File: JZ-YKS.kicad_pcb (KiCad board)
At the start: 2 copper layers, 50 x 50 mm, 50 parts, among them IC1 JZ4725, J1 USB_MINIB, U1 PINHEAD30, U2 PINHEAD30, U4 HY27UG088G5M, U5 P3V56S40ETP-G6, X1 CRYSTAL, X2 CRYSTAL

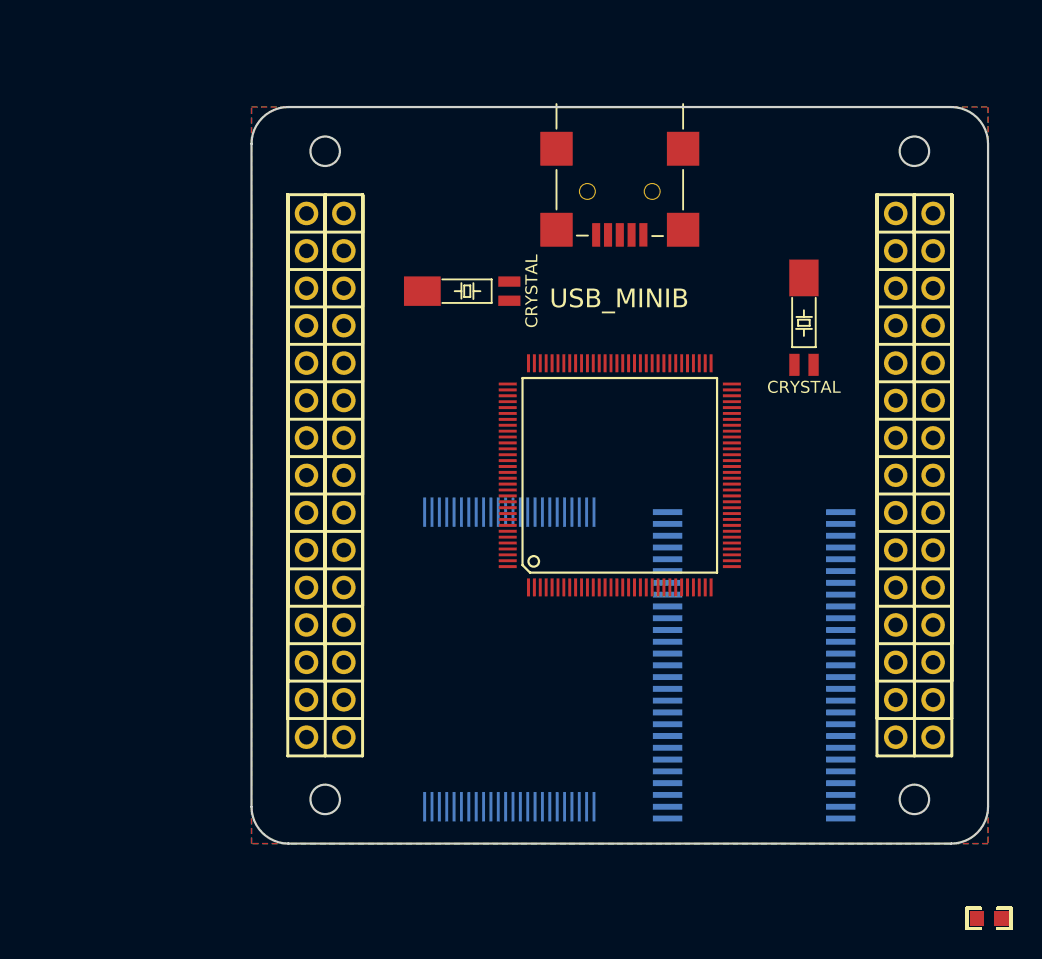
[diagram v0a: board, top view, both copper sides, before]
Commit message: another layout with funky 45 degree rotation
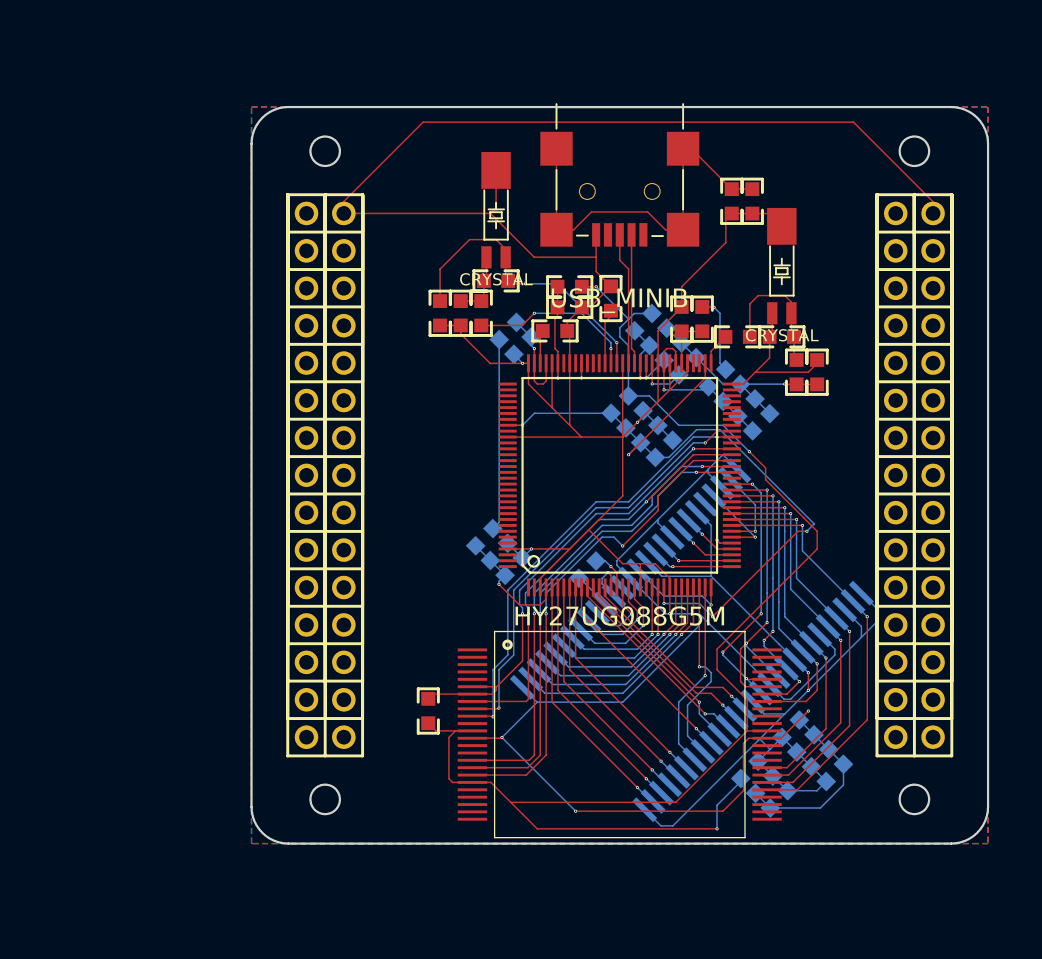
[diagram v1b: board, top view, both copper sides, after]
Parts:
- C10, C11, C12, C13, C14, C2, C21, C22, C23, C24, C25, C26, C3, C4, C5, C6, C7, FB1, FB2, FB4, FB5, FB7, FB9, R1, R6: moved to B.Cu
- U4: moved to F.Cu
- moved C18 55.5 mm to (137.8, 94.0), turned to 270 degrees
- moved R4 54.7 mm to (141.6, 91.8)
- moved C17 54.5 mm to (139.2, 94.0), turned to 270 degrees
- moved R2 53.6 mm to (140.6, 94.0), turned to 90 degrees
- moved C20 51.7 mm to (157.6, 86.4), turned to 90 degrees
- moved FB4 51.6 mm to (142.4, 95.2), turned to 225 degrees
- moved FB6 51.5 mm to (146.6, 92.2)
- moved FB8 51.3 mm to (159.0, 86.4), turned to 90 degrees
- moved C15 50.3 mm to (146.6, 93.6)
- moved C11 50.1 mm to (143.4, 96.2), turned to 225 degrees
- moved C8 49.6 mm to (145.6, 95.2)
- moved C1 49.3 mm to (149.4, 93.0), turned to 90 degrees
- moved FB5 46.8 mm to (151.6, 94.6), turned to 45 degrees
- moved C9 45.7 mm to (154.2, 94.4), turned to 90 degrees
- moved C10 45.4 mm to (152.6, 95.6), turned to 45 degrees
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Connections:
- IC1 pad 100: (no net) -> N-00000103
- IC1 pad 101: (no net) -> N-00000104
- IC1 pad 108: (no net) -> VSYN
- IC1 pad 109: (no net) -> HSYN
- IC1 pad 110: (no net) -> DE
- IC1 pad 2: (no net) -> PCLK
- IC1 pad 48: (no net) -> PWM
- IC1 pad 54: (no net) -> SD_CD
- IC1 pad 57: (no net) -> RXD
- IC1 pad 58: (no net) -> TXD
- IC1 pad 59: (no net) -> SCK
- IC1 pad 60: (no net) -> SDA
- IC1 pad 61: (no net) -> SD_DO
- IC1 pad 62: (no net) -> SD_CLK
- IC1 pad 63: (no net) -> SD_CMD
- IC1 pad 67: (no net) -> ADIN0
- IC1 pad 68: (no net) -> ADIN1
- IC1 pad 84: (no net) -> N-00000109
- IC1 pad 85: (no net) -> N-00000108
- IC1 pad 86: (no net) -> N-00000107
- IC1 pad 88: (no net) -> HP_R
- IC1 pad 90: (no net) -> HP_L
- IC1 pad 97: (no net) -> IN_L
- IC1 pad 98: (no net) -> IN_R
- IC1 pad 99: (no net) -> MIC
- J1 pad 1: (no net) -> VCC
- J1 pad 4: (no net) -> N-0000025
- U1 pad 10: B7 -> N-00000168
- U1 pad 11: G0 -> N-00000165
- U1 pad 12: G1 -> N-00000150
- U1 pad 13: G2 -> N-00000162
- U1 pad 14: G3 -> N-00000160
- U1 pad 15: G4 -> N-00000158
- U1 pad 16: G5 -> N-00000156
- U1 pad 17: G6 -> N-00000154
- U1 pad 18: G7 -> N-00000152
- U1 pad 19: (no net) -> N-00000147
- U1 pad 20: R1 -> N-00000167
- U1 pad 21: R2 -> N-00000164
- U1 pad 22: R3 -> N-00000163
- U1 pad 23: R4 -> N-00000161
- U1 pad 24: R5 -> N-00000159
- U1 pad 25: R6 -> N-00000157
- U1 pad 26: R7 -> N-00000155
- U1 pad 27: (no net) -> N-00000153
- U1 pad 28: (no net) -> N-00000151
- U1 pad 29: (no net) -> N-00000149
- U1 pad 3: (no net) -> N-00000148
- U1 pad 30: (no net) -> N-00000166
- U1 pad 4: B1 -> N-00000174
- U1 pad 5: B2 -> N-00000173
- U1 pad 6: B3 -> N-00000172
- U1 pad 7: B4 -> N-00000171
- U1 pad 8: B5 -> N-00000170
- U1 pad 9: B6 -> N-00000169
- U2 pad 10: (no net) -> N-00000145
- U2 pad 11: (no net) -> N-00000142
- U2 pad 12: (no net) -> N-00000140
- U2 pad 13: (no net) -> N-00000138
- U2 pad 14: (no net) -> N-00000136
- U2 pad 15: (no net) -> N-00000134
- U2 pad 16: (no net) -> N-00000132
- U2 pad 17: (no net) -> N-00000130
- U2 pad 18: (no net) -> N-00000128
- U2 pad 19: (no net) -> N-00000126
- U2 pad 20: (no net) -> N-00000144
- U2 pad 21: (no net) -> N-00000141
- U2 pad 22: (no net) -> N-00000139
- U2 pad 23: (no net) -> N-00000137
- U2 pad 24: (no net) -> N-00000135
- U2 pad 25: (no net) -> N-00000124
- U2 pad 26: (no net) -> N-00000131
- U2 pad 27: (no net) -> N-00000129
- U2 pad 28: (no net) -> N-00000127
- U2 pad 29: (no net) -> N-00000125
- U2 pad 3: (no net) -> N-00000120
- U2 pad 30: (no net) -> N-00000143
- U2 pad 4: (no net) -> N-00000121
- U2 pad 5: (no net) -> N-00000122
- U2 pad 6: (no net) -> N-00000123
- U2 pad 7: (no net) -> N-00000119
- U2 pad 8: (no net) -> N-00000133
- U2 pad 9: (no net) -> N-00000146
- U4 pad 1: (no net) -> N-00000191
- U4 pad 11: (no net) -> N-00000184
- U4 pad 14: (no net) -> N-00000201
- U4 pad 15: (no net) -> N-00000192
- U4 pad 2: (no net) -> N-00000190
- U4 pad 20: (no net) -> N-00000186
- U4 pad 21: (no net) -> N-00000183
- U4 pad 22: (no net) -> N-00000182
- U4 pad 23: (no net) -> N-00000203
- U4 pad 24: (no net) -> N-00000200
- U4 pad 25: (no net) -> N-00000198
- U4 pad 26: (no net) -> N-00000195
- U4 pad 27: (no net) -> N-00000193
- U4 pad 28: (no net) -> N-00000180
- U4 pad 3: (no net) -> N-00000189
- U4 pad 33: (no net) -> N-00000202
- U4 pad 34: (no net) -> N-00000199
- U4 pad 35: (no net) -> N-00000197
- U4 pad 38: (no net) -> N-00000179
- U4 pad 39: (no net) -> N-00000177
- U4 pad 4: (no net) -> N-00000188
- U4 pad 40: (no net) -> N-00000185
- U4 pad 45: (no net) -> N-00000196
- U4 pad 46: (no net) -> N-00000194
- U4 pad 47: (no net) -> N-00000181
- U4 pad 48: (no net) -> N-00000178
- U4 pad 5: (no net) -> N-00000187
- U5 pad 40: (no net) -> N-00000176
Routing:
- net GND: track 0.00 -> 287.5 mm, vias 0 -> 8
- net +3.3V: track 0.00 -> 95.6 mm, vias 0 -> 3
- net N-00000204: track 0.00 -> 62.6 mm, vias 0 -> 2
- net N-00000106: track 0.00 -> 49.6 mm, vias 0 -> 5
- net FWE: track 0.00 -> 34.0 mm, vias 0 -> 2
- net A16: track 0.00 -> 32.7 mm, vias 0 -> 2
- net A15: track 0.00 -> 32.7 mm, vias 0 -> 2
- net FRB: track 0.00 -> 32.5 mm, vias 0 -> 2
- net CS2: track 0.00 -> 30.0 mm, vias 0 -> 2
- net CS1: track 0.00 -> 29.5 mm, vias 0 -> 2
- net FRE: track 0.00 -> 29.0 mm, vias 0 -> 2
- net D0: track 0.00 -> 28.6 mm, vias 0 -> 2
- net D1: track 0.00 -> 27.1 mm, vias 0 -> 2
- net N-0000086: track 0.00 -> 26.4 mm
- net D2: track 0.00 -> 26.1 mm, vias 0 -> 2
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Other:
- net class Default: clearance 0.254 -> 0.1; trace_width 0.254 -> 0.1; via_dia 0.889 -> 0.21; via_drill 0.635 -> 0.2
- rule trace_clearance: 0.254 -> 0.1
- rule trace_min: 0.254 -> 0.1
- rule via_min_drill: 0.508 -> 0.2
- rule via_min_size: 0.889 -> 0.21

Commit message: fixed wrong voltage and some improvements
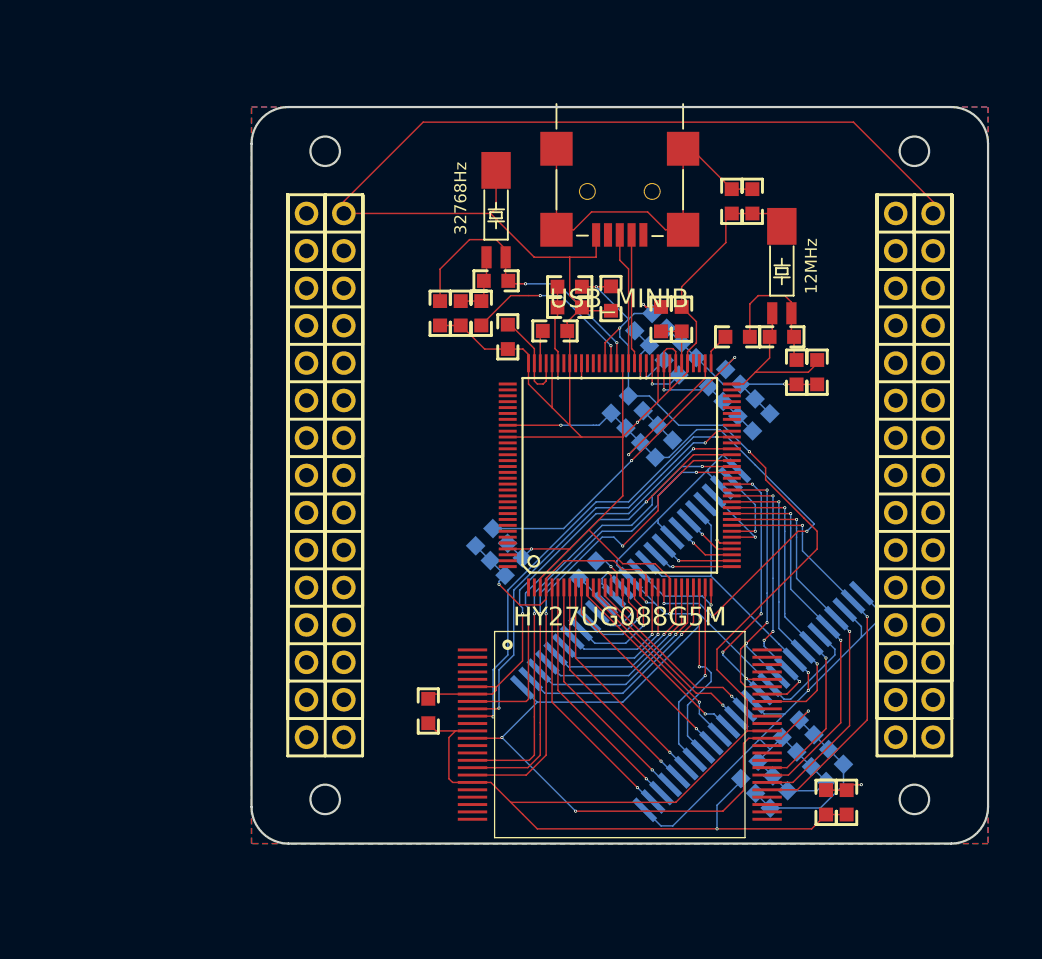
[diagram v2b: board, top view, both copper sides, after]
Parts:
- removed FB4: FB, size-0603
- added C27: 0.1uF, size-0603, F.Cu at (164.0, 127.2)
- added C28: 10uF, size-0603, F.Cu at (165.4, 127.2)
- C1, C13, C21, C22, C23, C24, C25, C3, C4, C5, C9: value C -> 0.1uF
- C10, C7, C8: value C -> 1uF
- C11: value C -> 0.01uF; moved to F.Cu
- C12: value C -> 0.01uF
- C14, C15, C2, C26, C6: value C -> 10uF
- C16, C17, C18, C19: value C -> 22pF
- FB1, FB2, FB3, FB5, FB6, FB7, FB8, FB9: value FB -> BKP1608HS121
- R1: value R -> 10k
- R2, R3, R6: value R -> 33
- R4: value R -> 10M
- R5: value R -> 1M
- R7: value R -> 100k
- X1: value CRYSTAL -> 32768Hz
- X2: value CRYSTAL -> 12MHz
- moved FB3 2.80 mm to (152.8, 94.4)
- moved C11 1.17 mm to (142.4, 95.6), turned to 270 degrees
- turned C1 to 270 degrees
- renumbered U4 to ?
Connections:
- C1 pad 1: VRTC -> +3.3V
- C11 pad 1: N-000005 -> +3.3V
- FB3 pad 2: +1.8V -> +3.3V
- IC1 pad 83: VRTC -> +3.3V
- IC1 pad 93: N-000005 -> +3.3V
- IC1 pad 95: N-000005 -> +3.3V
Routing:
- net +3.3V: track 95.6 -> 117.6 mm, vias 3 -> 5
- net N-00000101: track 8.35 -> 17.5 mm
- net N-000005: track 6.66 -> 0.00 mm, vias 1 -> 0
- net +1.8V: track 18.4 -> 22.3 mm, vias 1 -> 2
- net GND: track 287.5 -> 291.4 mm, vias 8 -> 9
- net VRTC: track 3.73 -> 0.00 mm
- net N-000002: track 11.4 -> 12.3 mm

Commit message: pinheads are now connected
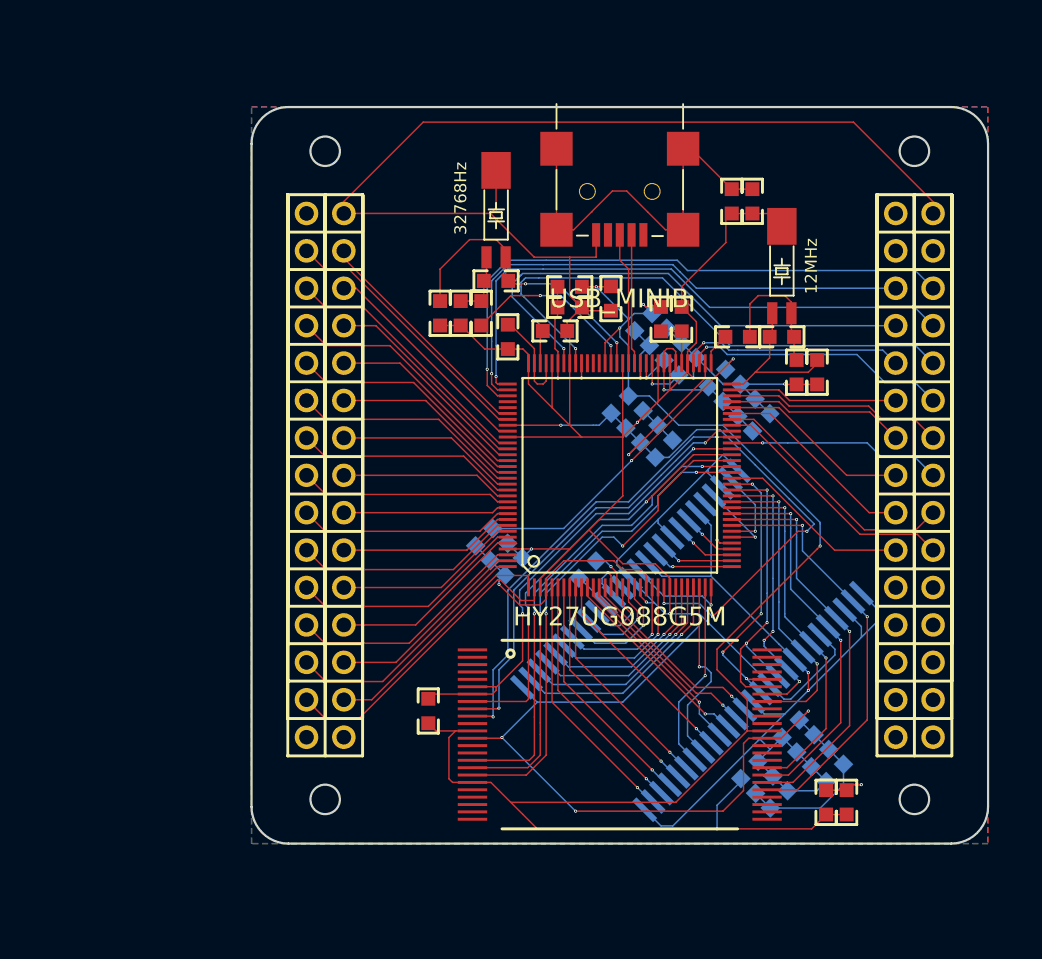
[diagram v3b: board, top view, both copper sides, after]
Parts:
- removed ?: HY27UG088G5M, TSOP48
- added U4: HY27UG088G5M, TSOP48, F.Cu at (150.0, 122.6)
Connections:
- U1 pad 10: N-00000166 -> R7
- U1 pad 11: N-00000163 -> R6
- U1 pad 12: N-00000148 -> R5
- U1 pad 13: N-00000160 (its old number) -> R4
- U1 pad 14: N-00000158 -> R3
- U1 pad 15: N-00000156 -> R2
- U1 pad 16: N-00000154 -> G7
- U1 pad 17: N-00000152 -> G6
- U1 pad 18: N-00000150 -> G5
- U1 pad 19: N-00000145 -> G4
- U1 pad 20: N-00000165 -> G3
- U1 pad 21: N-00000162 -> G2
- U1 pad 22: N-00000161 -> B7
- U1 pad 23: N-00000159 -> B6
- U1 pad 24: N-00000157 -> B5
- U1 pad 25: N-00000155 -> B4
- U1 pad 26: N-00000153 -> B3
- U1 pad 27: N-00000151 -> B2
- U1 pad 28: N-00000149 -> PCLK
- U1 pad 3: N-00000146 -> G0
- U1 pad 4: N-00000172 -> R1
- U1 pad 5: N-00000171 -> B1
- U1 pad 6: N-00000170 -> G1
- U1 pad 7: N-00000169 -> VSYN
- U1 pad 8: N-00000168 -> HSYN
- U1 pad 9: N-00000167 -> DE
- U2 pad 10: N-00000143 -> ADIN1
- U2 pad 11: N-00000140 -> ADIN0
- U2 pad 12: N-00000138 -> SD_CMD
- U2 pad 13: N-00000136 -> SD_CLK
- U2 pad 14: N-00000134 -> SD_DO
- U2 pad 15: N-00000132 (its old number) -> SD_CD
- U2 pad 16: N-00000130 (its old number) -> SDA
- U2 pad 17: N-00000128 (its old number) -> TXD
- U2 pad 18: N-00000126 (its old number) -> SCK
- U2 pad 19: N-00000124 (its old number) -> RXD
- U2 pad 20: N-00000142 -> PWM
- U2 pad 5: N-00000118 (its old number) -> MIC
- U2 pad 6: N-00000117 (its old number) -> IN_R
- U2 pad 7: N-00000121 (its old number) -> IN_L
- U2 pad 8: N-00000131 (its old number) -> HP_L
- U2 pad 9: N-00000144 -> HP_R
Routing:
- net MIC: track 0.00 -> 40.4 mm, vias 0 -> 1
- net IN_L: track 0.00 -> 39.3 mm, vias 0 -> 1
- net HP_R: track 0.00 -> 37.5 mm, vias 0 -> 1
- net IN_R: track 0.00 -> 36.8 mm, vias 0 -> 1
- net HP_L: track 0.00 -> 34.6 mm, vias 0 -> 1
- net PCLK: track 0.00 -> 21.4 mm
- net R1: track 0.00 -> 18.4 mm
- net ADIN0: track 0.00 -> 18.2 mm, vias 0 -> 1
- net G1: track 0.00 -> 18.0 mm
- net B3: track 0.00 -> 17.4 mm
- net HSYN: track 0.00 -> 17.3 mm
- net TXD: track 0.00 -> 17.2 mm
- net RXD: track 0.00 -> 17.2 mm
- net B2: track 0.00 -> 16.8 mm
- net B5: track 0.00 -> 16.7 mm
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
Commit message: final version of the board (goes to production)
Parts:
- added C29: C, size-0603, F.Cu at (163.8, 91.0)
- added C30: C, size-0603, F.Cu at (167.2, 85.0)
- added C31: C, size-0603, F.Cu at (166.2, 91.0)
- added U3: VREG-DUAL, sot23-6, F.Cu at (165.0, 87.2)
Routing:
- net +3.3V: track 117.8 -> 167.8 mm, vias 5 -> 10
- net GND: track 294.0 -> 312.3 mm
- net VCC: track 0.00 -> 17.3 mm
- net +1.8V: track 22.0 -> 37.9 mm

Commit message: that fucking TSOP library is all wrong
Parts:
- removed C1, C13, C3, C4, C5, C9: 0.1uF, size-0603
- removed C10, C7, C8: 1uF, size-0603
- removed C11, C12: 0.01uF, size-0603
- removed C14, C15, C2, C6: 10uF, size-0603
- removed C16, C17, C18, C19: 22pF, size-0603
- removed C20, C29, C30, C31: C, size-0603
- removed FB1, FB2, FB3, FB5, FB6, FB7, FB8: BKP1608HS121, size-0603
- removed R1: 10k, size-0603
- removed R2, R3: 33, size-0603
- removed R4: 10M, size-0603
- removed R5: 1M, size-0603
- removed U1, U2: PINHEAD30, PINHEAD30
- removed U3: VREG-DUAL, sot23-6
- removed X1: 32768Hz, crystal
- removed X2: 12MHz, crystal
- C21, C22, C23, C24, C25, C26, FB9, R6: moved to F.Cu
- R7: moved to B.Cu
- U4: footprint TSOP48 -> tsop48; moved to B.Cu
- U5: footprint TSOP54 -> tsop54
- moved U5 36.5 mm to (130.0, 115.0), turned to 180 degrees
- moved R7 30.7 mm to (142.7, 90.8), turned to 270 degrees
- moved U4 22.6 mm to (150.0, 100.0), turned to 0 degrees
- moved C28 20.1 mm to (151.1, 113.0), turned to 180 degrees
- moved C27 17.8 mm to (151.1, 114.9), turned to 180 degrees
- moved IC1 15.8 mm to (135.0, 100.0)
- moved J1 15.8 mm to (135.0, 75.0)
- moved FB9 15.0 mm to (153.0, 111.1), turned to 180 degrees
- moved C26 14.0 mm to (151.1, 116.8), turned to 180 degrees
- moved R6 11.9 mm to (136.1, 113.3)
- moved C24 11.6 mm to (154.9, 118.7), turned to 0 degrees
- moved C23 11.4 mm to (154.9, 116.8), turned to 0 degrees
- moved C21 11.3 mm to (154.9, 113.0), turned to 0 degrees
- moved C25 11.3 mm to (151.1, 118.7), turned to 180 degrees
- moved C22 11.3 mm to (154.9, 114.9), turned to 0 degrees
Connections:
- J1 pad 6: N-0000081 -> GND
- J1 pad 7: N-0000081 -> GND
- J1 pad 8: N-0000081 -> GND
- J1 pad 9: N-0000081 -> GND
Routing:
- net GND: track 312.3 -> 0.00 mm, vias 10 -> 0
- net +3.3V: track 167.8 -> 52.4 mm, vias 10 -> 3
- net N-00000159: track 62.6 -> 21.1 mm
- net MIC: track 40.4 -> 0.00 mm, vias 1 -> 0
- net IN_L: track 39.3 -> 0.00 mm, vias 1 -> 0
- net +1.8V: track 37.9 -> 0.00 mm, vias 2 -> 0
- net HP_R: track 37.5 -> 0.00 mm, vias 1 -> 0
- net IN_R: track 36.8 -> 0.00 mm, vias 1 -> 0
- net HP_L: track 34.6 -> 0.00 mm, vias 1 -> 0
- net D7: track 19.4 -> 47.4 mm, vias 4 -> 1
- net N-0000081: track 27.6 -> 0.00 mm
- net D6: track 21.3 -> 44.4 mm, vias 3 -> 1
- net D5: track 19.2 -> 42.0 mm, vias 4 -> 1
- net N-00000101: track 49.6 -> 27.1 mm, vias 5 -> 2
- net PCLK: track 21.4 -> 0.00 mm
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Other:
- outline, holes or cut-outs redrawn
- net class Default: clearance 0.1 -> 0.1524; trace_width 0.1 -> 0.1524; via_dia 0.21 -> 0.508; via_drill 0.2 -> 0.3302
- net class Power added: clearance 0.3048, trace_width 0.3048, via_dia 0.508, via_drill 0.3302
- rule trace_clearance: 0.1 -> 0.1524
- rule trace_min: 0.1 -> 0.1524
- rule via_min_drill: 0.2 -> 0.3302
- rule via_min_size: 0.21 -> 0.508

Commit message: rebirth of the pcb
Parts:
- removed C21, C22, C23, C24, C25, C27: 0.1uF, size-0603
- removed C26, C28: 10uF, size-0603
- removed FB9: BKP1608HS121, size-0603
- removed IC1: JZ4725, JZ-LQFP128
- removed J1: USB_MINIB, CON_USB_MB
- removed R6: 33, size-0603
- removed R7: 100k, size-0603
- removed U4: HY27UG088G5M, tsop48
- removed U5: P3V56S40ETP-G6, tsop54
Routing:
- net +3.3V: track 52.4 -> 0.00 mm, vias 3 -> 0
- net D7: track 47.4 -> 0.00 mm, vias 1 -> 0
- net D6: track 44.4 -> 0.00 mm, vias 1 -> 0
- net D5: track 42.0 -> 0.00 mm, vias 1 -> 0
- net D4: track 38.6 -> 0.00 mm, vias 1 -> 0
- net D3: track 33.6 -> 0.00 mm, vias 1 -> 0
- net D2: track 29.9 -> 0.00 mm, vias 1 -> 0
- net D1: track 27.1 -> 0.00 mm, vias 1 -> 0
- net N-00000101: track 27.1 -> 0.00 mm, vias 2 -> 0
- net A14: track 26.1 -> 0.00 mm, vias 1 -> 0
- net D15: track 25.0 -> 0.00 mm, vias 1 -> 0
- net A13: track 24.6 -> 0.00 mm, vias 1 -> 0
- net D14: track 23.3 -> 0.00 mm, vias 1 -> 0
- net D0: track 22.4 -> 0.00 mm, vias 1 -> 0
- net D13: track 22.4 -> 0.00 mm, vias 1 -> 0
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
